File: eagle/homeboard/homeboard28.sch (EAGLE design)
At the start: 126 parts, among them IC1 XCF02S, IC2 25LC080SN, IC3 ATMEGA32U2-TQFP, Q5 BC848SMD, Q6 BC848SMD, Q7 BC848SMD, Q8 BC848SMD, T1 BSS138, T2 BC848, T3 BSS138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

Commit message: maybe final
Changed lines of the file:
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@@
 </segment>
 <segment>
+<wire x1="327.66" y1="40.64" x2="309.88" y2="40.64" width="0.1524" layer="91"/>
+<label x="322.58" y="40.64" size="1.778" layer="95" rot="MR0"/>
+<wire x1="276.86" y1="40.64" x2="294.64" y2="40.64" width="0.1524" layer="91"/>
+<label x="281.94" y="40.64" size="1.778" layer="95"/>
 <pinref part="R55" gate="G$1" pin="1"/>
 <pinref part="R56" gate="G$1" pin="1"/>
 <wire x1="292.1" y1="53.34" x2="314.96" y2="53.34" width="0.1524" layer="91"/>
 <label x="304.8" y="53.34" size="1.778" layer="95" rot="MR0"/>
-<pinref part="SV1" gate="G$1" pin="3"/>
-<wire x1="294.64" y1="40.64" x2="327.66" y2="40.64" width="0.1524" layer="91"/>
 <wire x1="327.66" y1="40.64" x2="327.66" y2="53.34" width="0.1524" layer="91"/>
 <wire x1="327.66" y1="53.34" x2="314.96" y2="53.34" width="0.1524" layer="91"/>
 <junction x="314.96" y="53.34"/>
-<pinref part="SV1" gate="G$1" pin="4"/>
-<wire x1="309.88" y1="40.64" x2="276.86" y2="40.64" width="0.1524" layer="91"/>
 <wire x1="276.86" y1="40.64" x2="276.86" y2="53.34" width="0.1524" layer="91"/>
 <wire x1="276.86" y1="53.34" x2="292.1" y2="53.34" width="0.1524" layer="91"/>
 <junction x="292.1" y="53.34"/>
+<pinref part="SV1" gate="G$1" pin="3"/>
+<pinref part="SV1" gate="G$1" pin="4"/>
 </segment>
 <segment>
-<wire x1="281.94" y1="17.78" x2="294.64" y2="17.78" width="0.1524" layer="91"/>
-<label x="281.94" y="17.78" size="1.778" layer="95"/>
-</segment>
-<segment>
-<wire x1="322.58" y1="17.78" x2="309.88" y2="17.78" width="0.1524" layer="91"/>
-<label x="322.58" y="17.78" size="1.778" layer="95" rot="MR0"/>
-</segment>
-<segment>

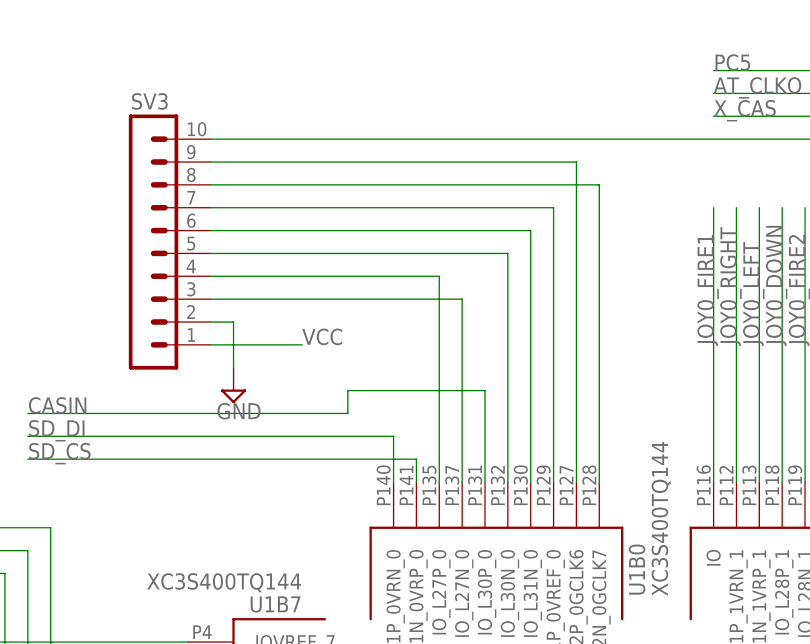
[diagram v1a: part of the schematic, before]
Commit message: all at 7mil
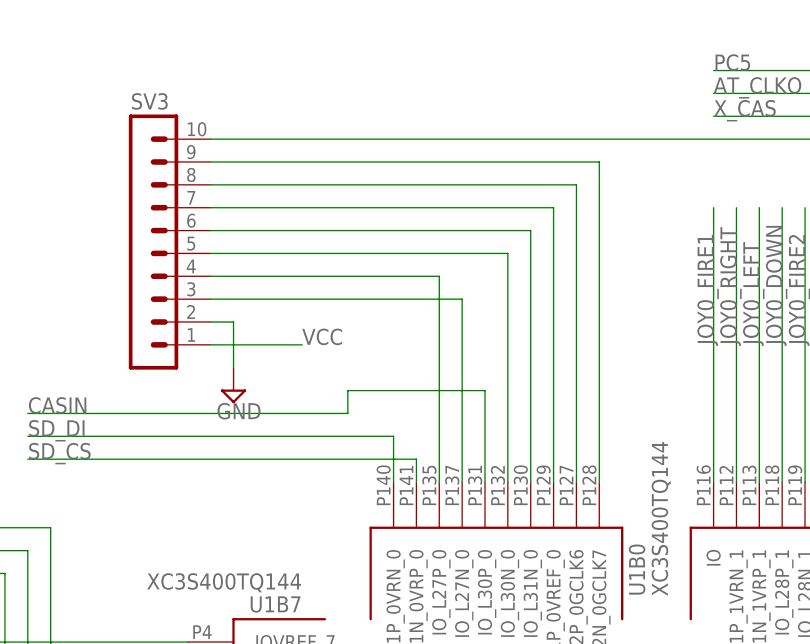
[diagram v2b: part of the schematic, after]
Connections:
- net N$6: now also SV3.9; no longer SV3.8
- net N$7: now also SV3.8; no longer SV3.9
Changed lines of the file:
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@@
 <net name="N$6" class="0">
 <segment>
-<pinref part="SV3" gate="1" pin="8"/>
 <pinref part="U1" gate="B0" pin="IO_L32N_0GCLK7"/>
-<wire x1="106.68" y1="106.68" x2="149.86" y2="106.68" width="0.1524" layer="91"/>
-<wire x1="149.86" y1="106.68" x2="149.86" y2="73.66" width="0.1524" layer="91"/>
+<wire x1="149.86" y1="109.22" x2="149.86" y2="73.66" width="0.1524" layer="91"/>
+<pinref part="SV3" gate="1" pin="9"/>
+<wire x1="106.68" y1="109.22" x2="149.86" y2="109.22" width="0.1524" layer="91"/>
 </segment>
 </net>
 <net name="N$7" class="0">
 <segment>
-<pinref part="SV3" gate="1" pin="9"/>
 <pinref part="U1" gate="B0" pin="IO_L32P_0GCLK6"/>
-<wire x1="106.68" y1="109.22" x2="147.32" y2="109.22" width="0.1524" layer="91"/>
-<wire x1="147.32" y1="109.22" x2="147.32" y2="73.66" width="0.1524" layer="91"/>
+<wire x1="147.32" y1="106.68" x2="147.32" y2="73.66" width="0.1524" layer="91"/>
+<pinref part="SV3" gate="1" pin="8"/>
+<wire x1="147.32" y1="106.68" x2="106.68" y2="106.68" width="0.1524" layer="91"/>
 </segment>
 </net>
